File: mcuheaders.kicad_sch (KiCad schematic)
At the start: 4 parts, among them J1 Left_02x24, J2 Right Header, J3 Right_02x24, J4 Left Header

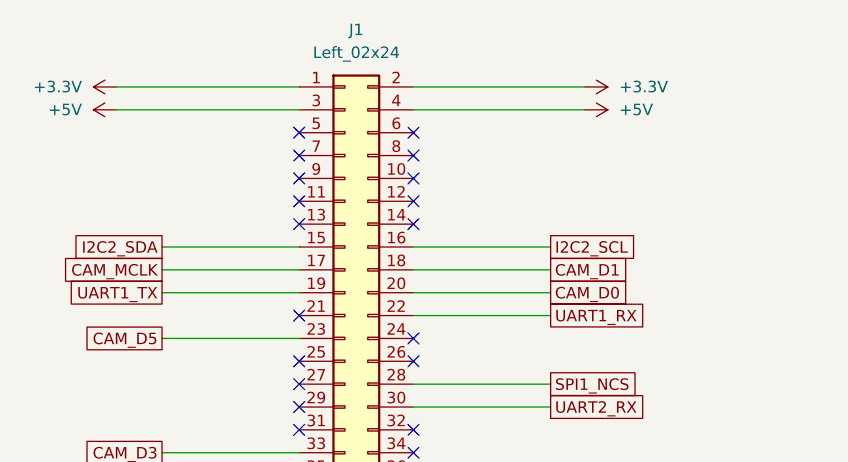
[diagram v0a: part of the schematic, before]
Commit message: fix missing SPI2 on TFT_SPI
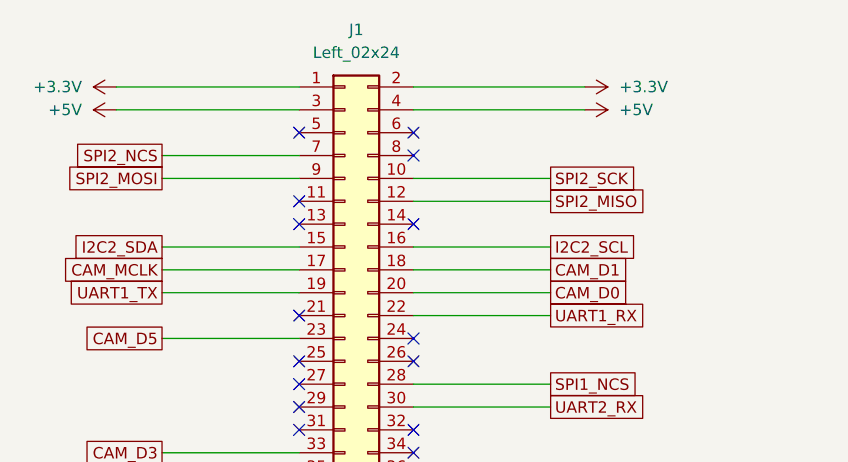
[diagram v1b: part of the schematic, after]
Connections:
- net SPI2_MISO: now also J1.12 (Pin_12)
- net SPI2_MOSI: now also J1.9 (Pin_9)
- net SPI2_NCS: now also J1.7 (Pin_7)
- net SPI2_SCK: now also J1.10 (Pin_10)
- no-connect marks 83 -> 79
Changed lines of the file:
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@@
 	)
 	(no_connect
-		(at 58.42 34.29)
+		(at 156.21 82.55)
 	)
 	(no_connect
@@
 	)
 	(no_connect
-		(at 71.12 39.37)
-	)
-	(no_connect
 		(at 156.21 54.61)
 	)
@@
 	)
 	(no_connect
-		(at 58.42 36.83)
-	)
-	(no_connect
 		(at 156.21 106.68)
 	)
@@
 	)
 	(no_connect
-		(at 71.12 36.83)
-	)
-	(no_connect
 		(at 71.12 74.93)
 	)
@@
 	)
 	(no_connect
-		(at 156.21 82.55)
-	)
-	(no_connect
 		(at 58.42 107.95)
 	)
@@
 	(wire
 		(pts
+			(xy 71.12 82.55) (xy 86.36 82.55)
+		)
+		(stroke
+			(width 0)
+			(type default)
+		)
+	)
+	(wire
+		(pts
 			(xy 43.18 74.93) (xy 58.42 74.93)
 		)
@@
 	(wire
 		(pts
+			(xy 43.18 36.83) (xy 58.42 36.83)
+		)
+		(stroke
+			(width 0)
+			(type default)
+		)
+	)
+	(wire
+		(pts
 			(xy 71.12 62.23) (xy 86.36 62.23)
 		)
@@
 	(wire
 		(pts
+			(xy 71.12 36.83) (xy 86.36 36.83)
+		)
+		(stroke
+			(width 0)
+			(type default)
+		)
+	)
+	(wire
+		(pts
 			(xy 43.18 46.99) (xy 58.42 46.99)
 		)
@@
 	(wire
 		(pts
+			(xy 43.18 34.29) (xy 58.42 34.29)
+		)
+		(stroke
+			(width 0)
+			(type default)
+		)
+	)
+	(wire
+		(pts
 			(xy 184.15 39.37) (xy 168.91 39.37)
 		)
@@
 	(wire
 		(pts
-			(xy 71.12 82.55) (xy 86.36 82.55)
-		)
-		(stroke
-			(width 0)
-			(type default)
-		)
-	)
-	(wire
-		(pts
 			(xy 43.18 49.53) (xy 58.42 49.53)
 		)
@@
 	(wire
 		(pts
+			(xy 71.12 39.37) (xy 86.36 39.37)
+		)
+		(stroke
+			(width 0)
+			(type default)
+		)
+	)
+	(wire
+		(pts
 			(xy 71.12 52.07) (xy 86.36 52.07)
 		)
@@
 		)
 	)
+	(global_label "SPI2_MOSI"
+		(shape passive)
+		(at 43.18 36.83 180)
+		(fields_autoplaced yes)
+		(effects
+			(font
+				(size 1.27 1.27)
+			)
+			(justify right)
+		)
+		(property "Intersheetrefs" "${INTERSHEET_REFS}"
+			(at 29.2259 36.83 0)
+			(effects
+				(font
+					(size 1.27 1.27)
+				)
+				(justify right)
+				(hide yes)
+			)
+		)
+	)
 	(global_label "SERVO_OUT2"
 		(shape passive)
@@
 		)
 	)
+	(global_label "SPI2_MISO"
+		(shape passive)
+		(at 86.36 39.37 0)
+		(fields_autoplaced yes)
+		(effects
+			(font
+				(size 1.27 1.27)
+			)
+			(justify left)
+		)
+		(property "Intersheetrefs" "${INTERSHEET_REFS}"
+			(at 100.3141 39.37 0)
+			(effects
+				(font
+					(size 1.27 1.27)
+				)
+				(justify left)
+				(hide yes)
+			)
+		)
+	)
 	(global_label "SPI2_MOSI"
 		(shape passive)
@@
 		)
 	)
+	(global_label "SPI2_SCK"
+		(shape passive)
+		(at 86.36 36.83 0)
+		(fields_autoplaced yes)
+		(effects
+			(font
+				(size 1.27 1.27)
+			)
+			(justify left)
+		)
+		(property "Intersheetrefs" "${INTERSHEET_REFS}"
+			(at 99.4674 36.83 0)
+			(effects
+				(font
+					(size 1.27 1.27)
+				)
+				(justify left)
+				(hide yes)
+			)
+		)
+	)
 	(global_label "UART1_RX"
 		(shape passive)
@@
 			(effects
 				(font
+					(size 1.27 1.27)
+				)
+				(justify right)
+				(hide yes)
+			)
+		)
+	)
+	(global_label "SPI2_NCS"
+		(shape passive)
+		(at 43.18 34.29 180)
+		(fields_autoplaced yes)
+		(effects
+			(font
+				(size 1.27 1.27)
+			)
+			(justify right)
+		)
+		(property "Intersheetrefs" "${INTERSHEET_REFS}"
+			(at 30.0121 34.29 0)
+			(effects
+				(font

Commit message: archive symbols to local Library.kicad_sym
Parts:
- J1, J3: symbol Connector_Generic:Conn_02x24_Odd_Even -> Library:Conn_02x24_Odd_Even
- J2, J4: symbol LM2676S-3.3_NOPB:Conn_02x22_Odd_Even -> Library:Conn_02x22_Odd_Even
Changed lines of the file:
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@@
 	)
 	(symbol
-		(lib_id "LM2676S-3.3_NOPB:Conn_02x22_Odd_Even")
+		(lib_id "Library:Conn_02x22_Odd_Even")
 		(at 63.5 125.73 0)
 		(unit 1)
@@
 	)
 	(symbol
-		(lib_id "Connector_Generic:Conn_02x24_Odd_Even")
+		(lib_id "Library:Conn_02x24_Odd_Even")
 		(at 161.29 54.61 0)
 		(unit 1)
@@
 	)
 	(symbol
-		(lib_id "Connector_Generic:Conn_02x24_Odd_Even")
+		(lib_id "Library:Conn_02x24_Odd_Even")
 		(at 63.5 54.61 0)
 		(unit 1)
@@
 	)
 	(symbol
-		(lib_id "LM2676S-3.3_NOPB:Conn_02x22_Odd_Even")
+		(lib_id "Library:Conn_02x22_Odd_Even")
 		(at 161.29 127 0)
 		(unit 1)
